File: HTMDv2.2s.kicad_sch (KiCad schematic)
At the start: 138 parts, among them IC1 TJA1441AT_0Z, IC2 A3921KLPTR-T, IC3 TMP275AQDGKRQ1, J1 Conn_01x04, J10 Conn_01x02, J11 Conn_01x02, J2 Conn_01x04, J3 Conn_01x06, J4 Conn_01x01, J5 Conn_01x01_Pin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

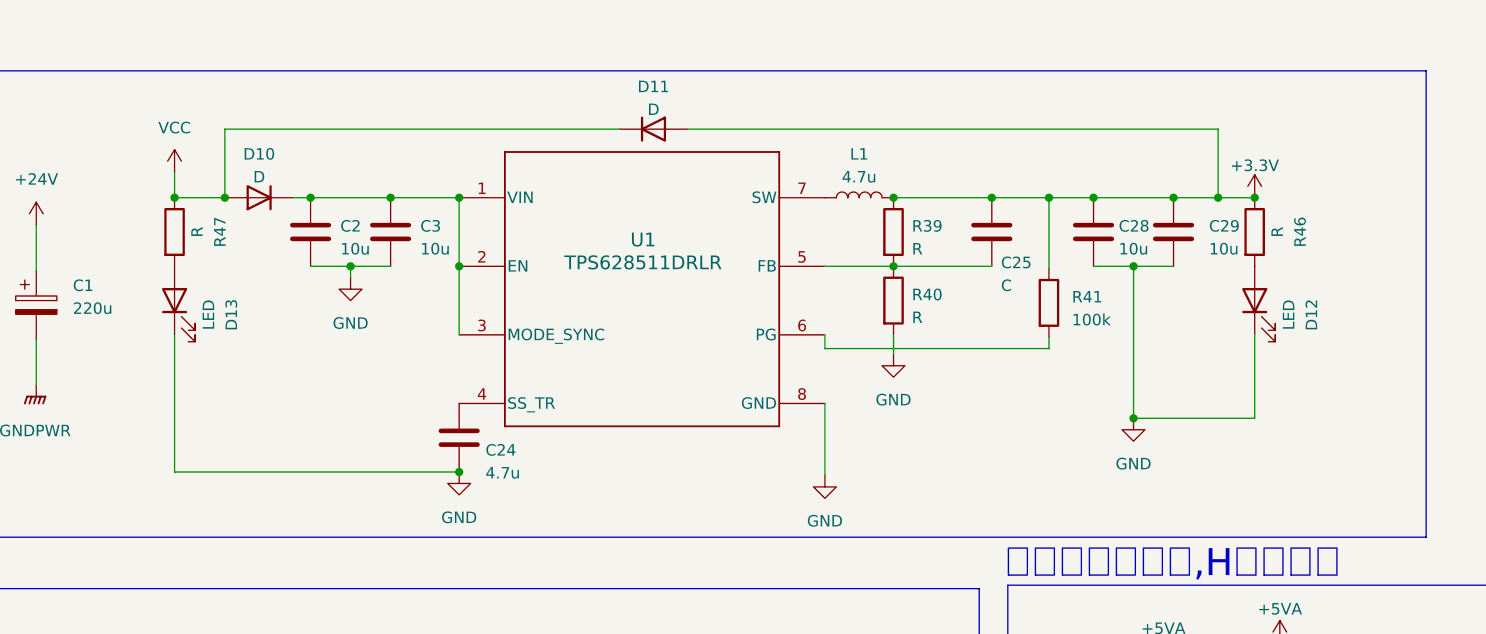
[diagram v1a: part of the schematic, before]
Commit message: Update HTMDv2.2s.kicad_sch
回路定数が間違っていたのを修正
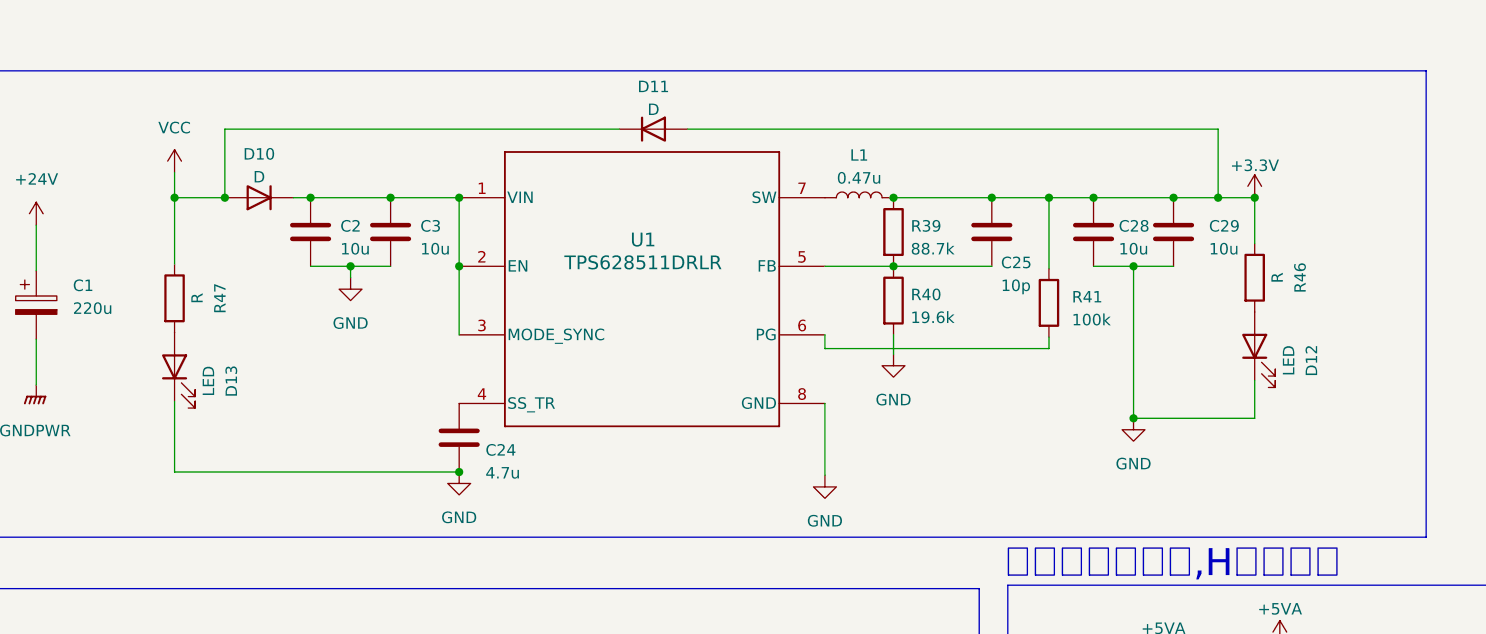
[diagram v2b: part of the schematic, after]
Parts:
- C25: value C -> 10p
- L1: value 4.7u -> 0.47u
- R39: value R -> 88.7k
- R40: value R -> 19.6k
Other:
- moved on the sheet: D12, D13, R46, R47
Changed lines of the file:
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@@
     (stroke (width 0) (type default))
   )
-  (wire (pts (xy 59.182 47.879) (xy 59.182 63.119))
+  (wire (pts (xy 59.182 55.245) (xy 59.182 63.119))
     (stroke (width 0) (type default))
   )
@@
     (stroke (width 0) (type default))
   )
+  (wire (pts (xy 179.197 37.719) (xy 179.197 32.639))
+    (stroke (width 0) (type default))
+  )
   (wire (pts (xy 182.118 136.144) (xy 182.118 105.029))
     (stroke (width 0) (type default))
@@
     (stroke (width 0) (type default))
   )
+  (wire (pts (xy 59.182 40.005) (xy 59.182 32.639))
+    (stroke (width 0) (type default))
+  )
   (wire (pts (xy 290.068 262.509) (xy 290.068 265.049))
     (stroke (width 0) (type default))
@@
     (stroke (width 0) (type default))
   )
-  (wire (pts (xy 179.197 47.879) (xy 179.197 57.15))
+  (wire (pts (xy 179.197 52.959) (xy 179.197 57.15))
     (stroke (width 0) (type default))
   )
@@
     )
   )
-  (symbol (lib_id "Device:R") (at 179.197 36.449 0) (unit 1)
+  (symbol (lib_id "Device:R") (at 179.197 41.529 0) (unit 1)
     (in_bom yes) (on_board yes) (dnp no) (fields_autoplaced)
-    (property "Reference" "R46" (at 184.277 36.449 90)
+    (property "Reference" "R46" (at 184.277 41.529 90)
       (effects (font (size 1.27 1.27)))
     )
-    (property "Value" "R" (at 181.737 36.449 90)
+    (property "Value" "R" (at 181.737 41.529 90)
       (effects (font (size 1.27 1.27)))
     )
-    (property "Footprint" "Resistor_SMD:R_0603_1608Metric_Pad0.98x0.95mm_HandSolder" (at 177.419 36.449 90)
+    (property "Footprint" "Resistor_SMD:R_0603_1608Metric_Pad0.98x0.95mm_HandSolder" (at 177.419 41.529 90)
       (effects (font (size 1.27 1.27)) hide)
     )
-    (property "Datasheet" "~" (at 179.197 36.449 0)
+    (property "Datasheet" "~" (at 179.197 41.529 0)
       (effects (font (size 1.27 1.27)) hide)
     )
@@
     )
   )
-  (symbol (lib_id "Device:LED") (at 179.197 44.069 90) (unit 1)
+  (symbol (lib_id "Device:LED") (at 179.197 49.149 90) (unit 1)
     (in_bom yes) (on_board yes) (dnp no) (fields_autoplaced)
-    (property "Reference" "D12" (at 185.547 45.6565 0)
+    (property "Reference" "D12" (at 185.547 50.7365 0)
       (effects (font (size 1.27 1.27)))
     )
-    (property "Value" "LED" (at 183.007 45.6565 0)
+    (property "Value" "LED" (at 183.007 50.7365 0)
       (effects (font (size 1.27 1.27)))
     )
-    (property "Footprint" "LED_SMD:LED_0603_1608Metric_Pad1.05x0.95mm_HandSolder" (at 179.197 44.069 0)
+    (property "Footprint" "LED_SMD:LED_0603_1608Metric_Pad1.05x0.95mm_HandSolder" (at 179.197 49.149 0)
       (effects (font (size 1.27 1.27)) hide)
     )
-    (property "Datasheet" "~" (at 179.197 44.069 0)
+    (property "Datasheet" "~" (at 179.197 49.149 0)
       (effects (font (size 1.27 1.27)) hide)
     )
@@
   (symbol (lib_id "Device:R") (at 139.065 44.069 0) (unit 1)
     (in_bom yes) (on_board yes) (dnp no) (fields_autoplaced)
-    (property "Reference" "R40" (at 141.097 43.434 0)
+    (property "Reference" "R40" (at 140.97 43.434 0)
       (effects (font (size 1.27 1.27)) (justify left))
     )
-    (property "Value" "R" (at 141.097 45.974 0)
+    (property "Value" "19.6k" (at 140.97 45.974 0)
       (effects (font (size 1.27 1.27)) (justify left))
     )
@@
     )
   )
-  (symbol (lib_id "Device:R") (at 59.182 36.449 0) (unit 1)
+  (symbol (lib_id "Device:R") (at 59.182 43.815 0) (unit 1)
     (in_bom yes) (on_board yes) (dnp no) (fields_autoplaced)
-    (property "Reference" "R47" (at 64.262 36.449 90)
+    (property "Reference" "R47" (at 64.262 43.815 90)
       (effects (font (size 1.27 1.27)))
     )
-    (property "Value" "R" (at 61.722 36.449 90)
+    (property "Value" "R" (at 61.722 43.815 90)
       (effects (font (size 1.27 1.27)))
     )
-    (property "Footprint" "Resistor_SMD:R_0603_1608Metric_Pad0.98x0.95mm_HandSolder" (at 57.404 36.449 90)
+    (property "Footprint" "Resistor_SMD:R_0603_1608Metric_Pad0.98x0.95mm_HandSolder" (at 57.404 43.815 90)
       (effects (font (size 1.27 1.27)) hide)
     )
-    (property "Datasheet" "~" (at 59.182 36.449 0)
+    (property "Datasheet" "~" (at 59.182 43.815 0)
       (effects (font (size 1.27 1.27)) hide)
     )
@@
   (symbol (lib_id "Device:L") (at 135.255 32.639 90) (unit 1)
     (in_bom yes) (on_board yes) (dnp no) (fields_autoplaced)
-    (property "Reference" "L1" (at 135.255 27.813 90)
+    (property "Reference" "L1" (at 135.255 27.94 90)
       (effects (font (size 1.27 1.27)))
     )
-    (property "Value" "4.7u" (at 135.255 30.353 90)
+    (property "Value" "0.47u" (at 135.255 30.48 90)
       (effects (font (size 1.27 1.27)))
     )
@@
   (symbol (lib_id "Device:R") (at 139.065 36.449 0) (unit 1)
     (in_bom yes) (on_board yes) (dnp no) (fields_autoplaced)
-    (property "Reference" "R39" (at 141.097 35.814 0)
+    (property "Reference" "R39" (at 140.97 35.814 0)
       (effects (font (size 1.27 1.27)) (justify left))
     )
-    (property "Value" "R" (at 141.097 38.354 0)
+    (property "Value" "88.7k" (at 140.97 38.354 0)
       (effects (font (size 1.27 1.27)) (justify left))
     )
@@
     )
   )
-  (symbol (lib_id "Device:LED") (at 59.182 44.069 90) (unit 1)
+  (symbol (lib_id "Device:LED") (at 59.182 51.435 90) (unit 1)
     (in_bom yes) (on_board yes) (dnp no) (fields_autoplaced)
-    (property "Reference" "D13" (at 65.532 45.6565 0)
+    (property "Reference" "D13" (at 65.532 53.0225 0)
       (effects (font (size 1.27 1.27)))
     )
-    (property "Value" "LED" (at 62.992 45.6565 0)
+    (property "Value" "LED" (at 62.992 53.0225 0)
       (effects (font (size 1.27 1.27)))
     )
-    (property "Footprint" "LED_SMD:LED_0603_1608Metric_Pad1.05x0.95mm_HandSolder" (at 59.182 44.069 0)
+    (property "Footprint" "LED_SMD:LED_0603_1608Metric_Pad1.05x0.95mm_HandSolder" (at 59.182 51.435 0)
       (effects (font (size 1.27 1.27)) hide)
     )
-    (property "Datasheet" "~" (at 59.182 44.069 0)
+    (property "Datasheet" "~" (at 59.182 51.435 0)
       (effects (font (size 1.27 1.27)) hide)
     )
@@
       (effects (font (size 1.27 1.27)) (justify left))
     )
-    (property "Value" "C" (at 151.003 42.418 0)
+    (property "Value" "10p" (at 151.003 42.418 0)
       (effects (font (size 1.27 1.27)) (justify left))
     )

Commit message: update
発注Done
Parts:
- H4: footprint MountingHole:MountingHole_3.2mm_M3 -> MountingHole:MountingHole_3.2mm_M3_DIN965_Pad
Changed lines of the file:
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@@
       (effects (font (size 1.27 1.27)) (justify left))
     )
-    (property "Footprint" "MountingHole:MountingHole_3.2mm_M3" (at 379.984 108.839 0)
+    (property "Footprint" "MountingHole:MountingHole_3.2mm_M3_DIN965_Pad" (at 379.984 108.839 0)
       (effects (font (size 1.27 1.27)) hide)
     )

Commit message: 回路の修正
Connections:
- net +3.3V: now also C15.1, C17.1, R17.1, R28.1, R29.1, R30.1, U5.5 (Vdd)
- net VCC: no longer C15.1, C17.1, R17.1, R28.1, R29.1, R30.1, U5.5 (Vdd)
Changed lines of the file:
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@@
-    )
-  )
-  (symbol (lib_id "power:VCC") (at 233.553 179.324 0) (unit 1)
-    (in_bom yes) (on_board yes) (dnp no)
-    (property "Reference" "#PWR061" (at 233.553 183.134 0)
-      (effects (font (size 1.27 1.27)) hide)
-    )
-    (property "Value" "VCC" (at 233.553 174.371 0)
-      (effects (font (size 1.27 1.27)))
-    )
-    (property "Footprint" "" (at 233.553 179.324 0)
-      (effects (font (size 1.27 1.27)) hide)
-    )
-    (property "Datasheet" "" (at 233.553 179.324 0)
-      (effects (font (size 1.27 1.27)) hide)
-    )
-    (pin "1")
-    (instances
-      (project "HTMDv2.2s"
-        (path "/b4476ce1-4dbe-4b8d-acdf-5a8a6cb2187e"
-          (reference "#PWR061") (unit 1)
-        )
-      )
-      (project "HTMDv1.3"
-        (path "/ba6e8f7f-5a8b-40bd-8573-0dda1fc2862b"
-          (reference "#PWR016") (unit 1)
-        )
-      )
     )
   )
@@
         (path "/b4476ce1-4dbe-4b8d-acdf-5a8a6cb2187e"
           (reference "D7") (unit 1)
-        )
-      )
-    )
-  )
-  (symbol (lib_id "power:VCC") (at 254 179.07 0) (unit 1)
-    (in_bom yes) (on_board yes) (dnp no)
-    (property "Reference" "#PWR064" (at 254 182.88 0)
-      (effects (font (size 1.27 1.27)) hide)
-    )
-    (property "Value" "VCC" (at 254 174.117 0)
-      (effects (font (size 1.27 1.27)))
-    )
-    (property "Footprint" "" (at 254 179.07 0)
-      (effects (font (size 1.27 1.27)) hide)
-    )
-    (property "Datasheet" "" (at 254 179.07 0)
-      (effects (font (size 1.27 1.27)) hide)
-    )
-    (pin "1")
-    (instances
-      (project "HTMDv2.2s"
-        (path "/b4476ce1-4dbe-4b8d-acdf-5a8a6cb2187e"
-          (reference "#PWR064") (unit 1)
-        )
-      )
-      (project "HTMDv1.3"
-        (path "/ba6e8f7f-5a8b-40bd-8573-0dda1fc2862b"
-          (reference "#PWR016") (unit 1)
         )
       )
@@
     )
   )
+  (symbol (lib_id "power:+3.3V") (at 233.553 179.324 0) (unit 1)
+    (in_bom yes) (on_board yes) (dnp no) (fields_autoplaced)
+    (property "Reference" "#PWR017" (at 233.553 183.134 0)
+      (effects (font (size 1.27 1.27)) hide)
+    )
+    (property "Value" "+3.3V" (at 233.553 174.244 0)
+      (effects (font (size 1.27 1.27)))
+    )
+    (property "Footprint" "" (at 233.553 179.324 0)
+      (effects (font (size 1.27 1.27)) hide)
+    )
+    (property "Datasheet" "" (at 233.553 179.324 0)
+      (effects (font (size 1.27 1.27)) hide)
+    )
+    (pin "1")
+    (instances
+      (project "HTMDv2.2s"
+        (path "/b4476ce1-4dbe-4b8d-acdf-5a8a6cb2187e"
+          (reference "#PWR017") (unit 1)
+        )
+      )
+    )
+  )
   (symbol (lib_id "0-Myparts:SQJ180EP-T1_GE3") (at 288.798 134.366 0) (unit 1)
     (in_bom yes) (on_board yes) (dnp no)
@@
     )
   )
+  (symbol (lib_id "power:+3.3V") (at 254 179.07 0) (unit 1)
+    (in_bom yes) (on_board yes) (dnp no) (fields_autoplaced)
+    (property "Reference" "#PWR018" (at 254 182.88 0)
+      (effects (font (size 1.27 1.27)) hide)
+    )
+    (property "Value" "+3.3V" (at 254 173.99 0)
+      (effects (font (size 1.27 1.27)))
+    )
+    (property "Footprint" "" (at 254 179.07 0)
+      (effects (font (size 1.27 1.27)) hide)
+    )
+    (property "Datasheet" "" (at 254 179.07 0)
+      (effects (font (size 1.27 1.27)) hide)
+    )
+    (pin "1")
+    (instances
+      (project "HTMDv2.2s"
+        (path "/b4476ce1-4dbe-4b8d-acdf-5a8a6cb2187e"
+          (reference "#PWR018") (unit 1)
+        )
+      )
+    )
+  )
   (symbol (lib_id "Device:R") (at 277.241 59.055 0) (unit 1)
     (in_bom yes) (on_board yes) (dnp no) (fields_autoplaced)
@@
     )
   )
+  (symbol (lib_id "power:+3.3V") (at 254.381 238.76 0) (unit 1)
+    (in_bom yes) (on_board yes) (dnp no) (fields_autoplaced)
+    (property "Reference" "#PWR010" (at 254.381 242.57 0)
+      (effects (font (size 1.27 1.27)) hide)
+    )
+    (property "Value" "+3.3V" (at 254.381 233.68 0)
+      (effects (font (size 1.27 1.27)))
+    )
+    (property "Footprint" "" (at 254.381 238.76 0)
+      (effects (font (size 1.27 1.27)) hide)
+    )
+    (property "Datasheet" "" (at 254.381 238.76 0)
+      (effects (font (size 1.27 1.27)) hide)
+    )
+    (pin "1")
+    (instances
+      (project "HTMDv2.2s"
+        (path "/b4476ce1-4dbe-4b8d-acdf-5a8a6cb2187e"
+          (reference "#PWR010") (unit 1)
+        )
+      )
+    )
+  )
   (symbol (lib_id "power:+3.3V") (at 284.226 180.975 0) (unit 1)
     (in_bom yes) (on_board yes) (dnp no) (fields_autoplaced)
@@
         )
       )
-    )
-  )
-  (symbol (lib_id "power:VCC") (at 254.381 238.76 0) (mirror y) (unit 1)
-    (in_bom yes) (on_board yes) (dnp no)
-    (property "Reference" "#PWR010" (at 254.381 242.57 0)
-      (effects (font (size 1.27 1.27)) hide)
-    )
-    (property "Value" "VCC" (at 254.381 233.807 0)
-      (effects (font (size 1.27 1.27)))
-    )
-    (property "Footprint" "" (at 254.381 238.76 0)
-      (effects (font (size 1.27 1.27)) hide)
-    )
-    (property "Datasheet" "" (at 254.381 238.76 0)
-      (effects (font (size 1.27 1.27)) hide)
-    )
-    (pin "1")
-    (instances
-      (project "HTMDv2.2s"
-        (path "/b4476ce1-4dbe-4b8d-acdf-5a8a6cb2187e"
-          (reference "#PWR010") (unit 1)
-        )
-      )
-      (project "HTMDv1.3"
-        (path "/ba6e8f7f-5a8b-40bd-8573-0dda1fc2862b"
-          (reference "#PWR016") (unit 1)
-        )
-      )

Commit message: prefin
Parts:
- removed D1, D14, D7, D8, D9: LED, LED_SMD:LED_0603_1608Metric_Pad1.05x0.95mm_HandSolder, symbol Device:LED
- removed R42, R43, R44, R45, R48: R, Resistor_SMD:R_0603_1608Metric_Pad0.98x0.95mm_HandSolder, symbol Device:R
- added SW1: SW_Coded, 0_Mylib:FR01FR16H-S, symbol Switch:SW_Coded
- U13, U14, U15, U16: footprint 0-Myparts:SQJ180EP-T1_GE3 -> Package_SO:PowerPAK_SO-8_Single
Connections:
- net +3.3V: now also SW1.1 (CM)
- net LED2: now also SW1.2 (D0)
- net LED3: now also SW1.3 (D1)
- net LED4: now also SW1.4 (D2)
- net LED5: now also SW1.5 (D3)
